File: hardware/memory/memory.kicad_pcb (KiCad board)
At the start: 2 copper layers, 77 x 77 mm, 76 parts, among them J1 Conn_Mem, J2 Conn_Power, J3 Conn_Mem_Ext, U1 74HC161, U10 74HC595, U11 74HC595, U12 74HC595, U13 74HC595, U14 74HC597, U15 74HC74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

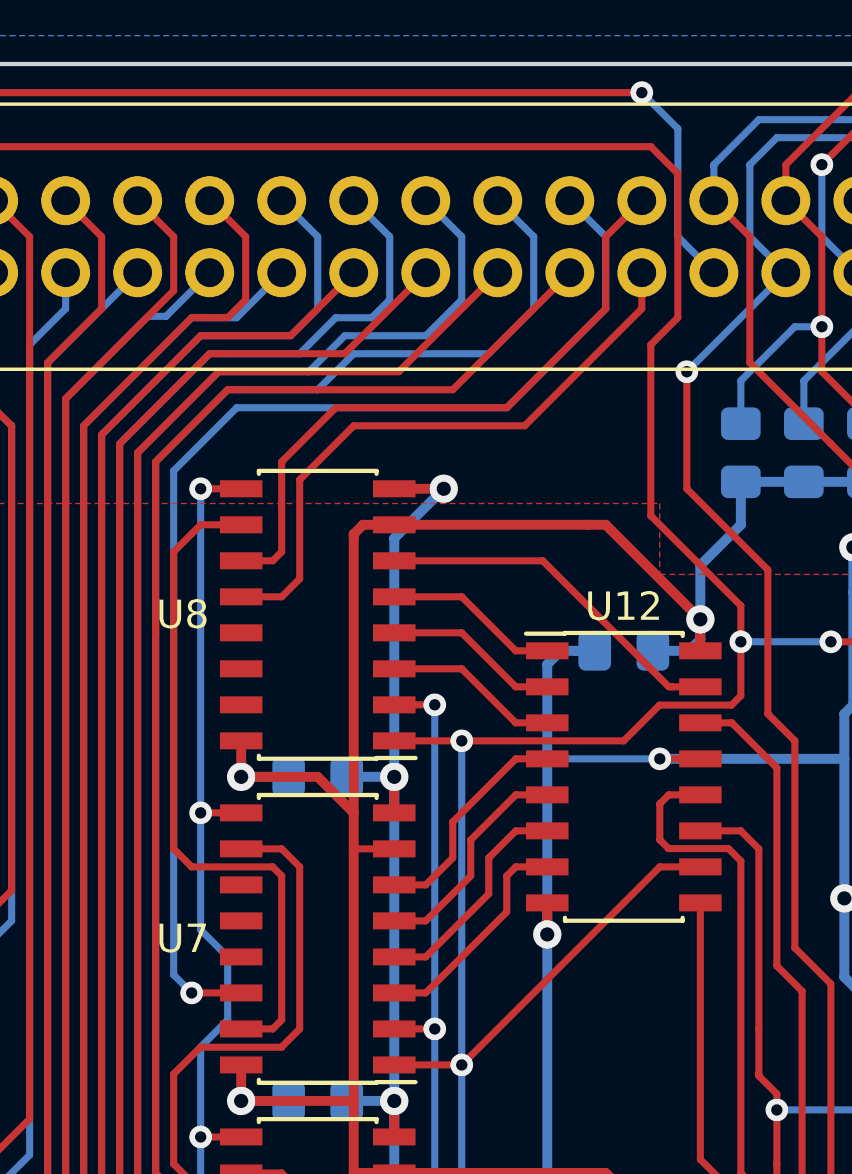
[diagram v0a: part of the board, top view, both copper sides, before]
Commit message: Added ~RESET to memory bus
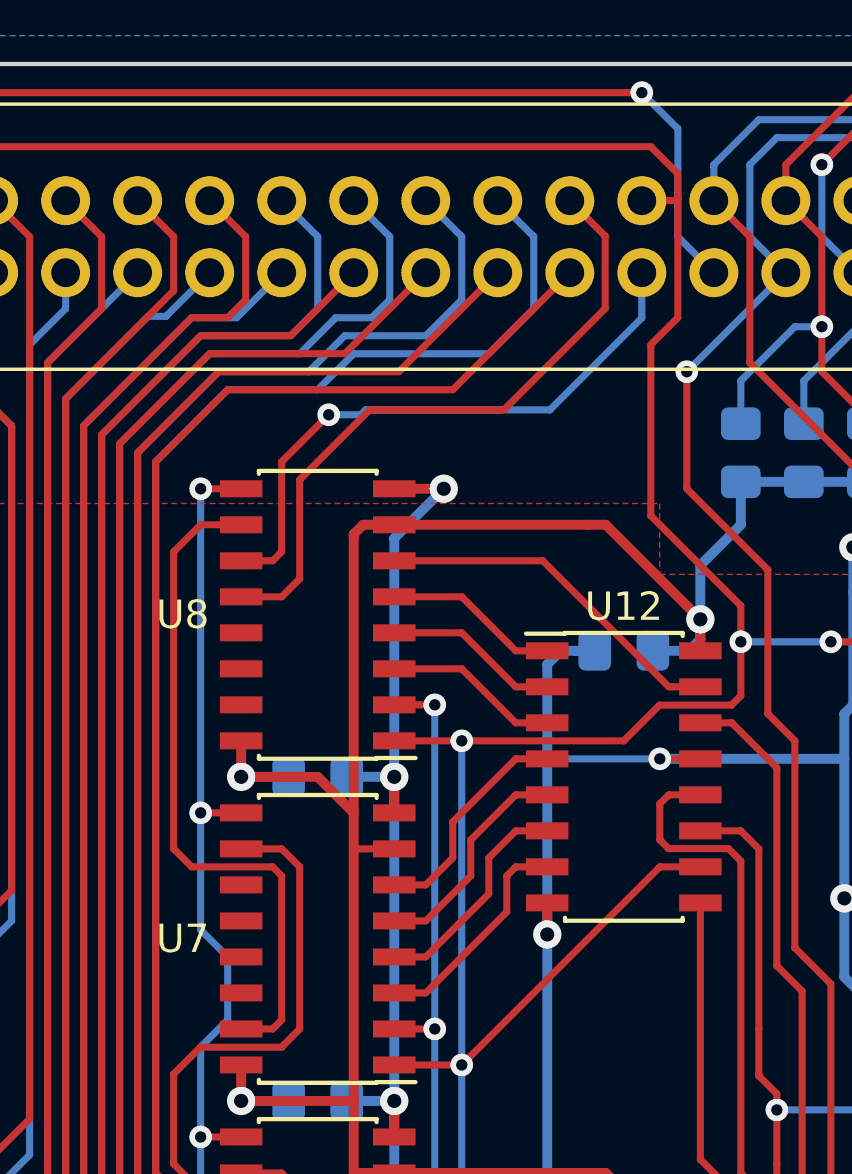
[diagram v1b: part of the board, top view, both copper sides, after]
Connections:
- J3 pad 26: /A24 -> /A30
- J3 pad 27: /A30 -> /A31
- J3 pad 28: /A31 -> /~RESET
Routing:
- net /A24: track 42.4 -> 0.00 mm, vias 1 -> 0
- net /A30: track 21.7 -> 23.4 mm
- net /A31: track 22.7 -> 21.1 mm, vias 0 -> 1
- net /~RESET: track 290.1 -> 291.4 mm
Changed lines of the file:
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@@
     (thickness 1.6)
     (drawings 17)
-    (tracks 1612)
+    (tracks 1610)
     (zones 0)
     (modules 76)
@@
       (net 102 /A23))
     (pad 26 thru_hole oval (at 2.54 30.48 90) (size 1.7272 1.7272) (drill 1.016) (layers *.Cu *.Mask)
-      (net 65 /A24))
-    (pad 27 thru_hole oval (at 0 33.02 90) (size 1.7272 1.7272) (drill 1.016) (layers *.Cu *.Mask)
       (net 57 /A30))
-    (pad 28 thru_hole oval (at 2.54 33.02 90) (size 1.7272 1.7272) (drill 1.016) (layers *.Cu *.Mask)
+    (pad 27 thru_hole oval (at 0 33.02 90) (size 1.7272 1.7272) (drill 1.016) (layers *.Cu *.Mask)
       (net 58 /A31))
+    (pad 28 thru_hole oval (at 2.54 33.02 90) (size 1.7272 1.7272) (drill 1.016) (layers *.Cu *.Mask)
+      (net 18 /~RESET))
     (pad 29 thru_hole oval (at 0 35.56 90) (size 1.7272 1.7272) (drill 1.016) (layers *.Cu *.Mask)
       (net 105 /~WAIT))
@@
   (segment (start 154.685 73.9325) (end 157.86 77.1075) (width 0.25) (layer F.Cu) (net 18))
   (segment (start 155.6375 66.9475) (end 154.685 67.9) (width 0.25) (layer F.Cu) (net 18))
-  (segment (start 155.6375 61.8675) (end 155.6375 66.9475) (width 0.25) (layer F.Cu) (net 18))
   (segment (start 154.685 67.9) (end 154.685 73.9325) (width 0.25) (layer F.Cu) (net 18))
   (segment (start 120.7125 71.075) (end 119.4425 69.805) (width 0.25) (layer F.Cu) (net 18))
@@
   (segment (start 149.3575 126.6825) (end 144.8425 126.6825) (width 0.25) (layer F.Cu) (net 18))
   (segment (start 144.2075 118.065) (end 144.2075 126.0475) (width 0.25) (layer F.Cu) (net 18))
+  (segment (start 155.6375 62.771314) (end 155.6375 62.725) (width 0.25) (layer F.Cu) (net 18))
+  (segment (start 155.588814 62.82) (end 155.6375 62.771314) (width 0.25) (layer F.Cu) (net 18))
+  (segment (start 154.3675 62.82) (end 155.588814 62.82) (width 0.25) (layer F.Cu) (net 18))
+  (segment (start 155.6375 61.8675) (end 155.6375 62.725) (width 0.25) (layer F.Cu) (net 18))
+  (segment (start 155.6375 62.725) (end 155.6375 66.9475) (width 0.25) (layer F.Cu) (net 18))
   (segment (start 156.4325 107.905) (end 159.13 107.905) (width 0.25) (layer F.Cu) (net 19))
   (segment (start 112.2975 81.235) (end 111.1875 81.235) (width 0.25) (layer F.Cu) (net 19))
@@
   (segment (start 118.49 90.76) (end 123.0925 90.76) (width 0.25) (layer F.Cu) (net 53))
   (segment (start 114.045 86.315) (end 118.49 90.76) (width 0.25) (layer F.Cu) (net 53))
-  (segment (start 141.6675 76.79) (end 140.2375 76.79) (width 0.25) (layer F.Cu) (net 57))
-  (segment (start 154.3675 65.36) (end 154.3675 66.63) (width 0.25) (layer F.Cu) (net 57))
-  (segment (start 142.3025 76.155) (end 141.6675 76.79) (width 0.25) (layer F.Cu) (net 57))
-  (segment (start 154.3675 66.63) (end 150.24 70.7575) (width 0.25) (layer F.Cu) (net 57))
-  (segment (start 150.24 70.7575) (end 144.2075 70.7575) (width 0.25) (layer F.Cu) (net 57))
-  (segment (start 144.2075 70.7575) (end 142.3025 72.6625) (width 0.25) (layer F.Cu) (net 57))
-  (segment (start 142.3025 72.6625) (end 142.3025 76.155) (width 0.25) (layer F.Cu) (net 57))
+  (segment (start 153.075 64.0675) (end 151.8275 62.82) (width 0.25) (layer F.Cu) (net 57))
+  (segment (start 153.075 66.625) (end 153.075 64.0675) (width 0.25) (layer F.Cu) (net 57))
+  (segment (start 141.6675 76.79) (end 142.3025 76.155) (width 0.25) (layer F.Cu) (net 57))
+  (segment (start 140.2375 76.79) (end 141.6675 76.79) (width 0.25) (layer F.Cu) (net 57))
+  (segment (start 142.3025 76.155) (end 142.3025 72.6625) (width 0.25) (layer F.Cu) (net 57))
+  (segment (start 144.765 70.2) (end 149.5 70.2) (width 0.25) (layer F.Cu) (net 57))
+  (segment (start 142.3025 72.6625) (end 144.765 70.2) (width 0.25) (layer F.Cu) (net 57))
+  (segment (start 149.5 70.2) (end 153.075 66.625) (width 0.25) (layer F.Cu) (net 57))
   (segment (start 141.35 75.52) (end 140.2375 75.52) (width 0.25) (layer F.Cu) (net 58))
   (segment (start 141.6675 75.2025) (end 141.35 75.52) (width 0.25) (layer F.Cu) (net 58))
-  (segment (start 154.3675 62.82) (end 153.0975 64.09) (width 0.25) (layer F.Cu) (net 58))
-  (segment (start 149.605 70.1225) (end 143.5725 70.1225) (width 0.25) (layer F.Cu) (net 58))
-  (segment (start 153.0975 66.63) (end 149.605 70.1225) (width 0.25) (layer F.Cu) (net 58))
-  (segment (start 153.0975 64.09) (end 153.0975 66.63) (width 0.25) (layer F.Cu) (net 58))
-  (segment (start 143.5725 70.1225) (end 141.6675 72.0275) (width 0.25) (layer F.Cu) (net 58))
   (segment (start 141.6675 72.0275) (end 141.6675 75.2025) (width 0.25) (layer F.Cu) (net 58))
+  (via (at 143.325 70.37) (size 0.8) (drill 0.4) (layers F.Cu B.Cu) (net 58))
+  (segment (start 143.325 70.37) (end 141.6675 72.0275) (width 0.25) (layer F.Cu) (net 58))
+  (segment (start 143.325 70.37) (end 144.455 70.37) (width 0.25) (layer B.Cu) (net 58))
+  (segment (start 144.455 70.37) (end 144.625 70.2) (width 0.25) (layer B.Cu) (net 58))
+  (segment (start 144.625 70.2) (end 151.125 70.2) (width 0.25) (layer B.Cu) (net 58))
+  (segment (start 154.3675 66.9575) (end 154.3675 65.36) (width 0.25) (layer B.Cu) (net 58))
+  (segment (start 151.125 70.2) (end 154.3675 66.9575) (width 0.25) (layer B.Cu) (net 58))
   (segment (start 138.81 74.25) (end 140.2375 74.25) (width 0.25) (layer F.Cu) (net 59))
   (segment (start 137.8575 75.2025) (end 138.81 74.25) (width 0.25) (layer F.Cu) (net 59))
@@
   (segment (start 140.2375 85.68) (end 141.6675 85.68) (width 0.25) (layer F.Cu) (net 61))
   (segment (start 142.3025 92.03) (end 142.3025 86.315) (width 0.25) (layer F.Cu) (net 61))
-  (segment (start 153.0975 64.09) (end 153.0975 66.63) (width 0.25) (layer B.Cu) (net 65))
-  (segment (start 140.08 70.1225) (end 137.8575 72.345) (width 0.25) (layer B.Cu) (net 65))
-  (segment (start 153.0975 66.63) (end 149.605 70.1225) (width 0.25) (layer B.Cu) (net 65))
-  (segment (start 151.8275 62.82) (end 153.0975 64.09) (width 0.25) (layer B.Cu) (net 65))
-  (segment (start 149.605 70.1225) (end 140.08 70.1225) (width 0.25) (layer B.Cu) (net 65))
-  (segment (start 137.8575 72.345) (end 137.8575 90.125) (width 0.25) (layer B.Cu) (net 65))
-  (segment (start 137.8575 90.125) (end 138.4925 90.76) (width 0.25) (layer B.Cu) (net 65))
-  (via (at 138.4925 90.76) (size 0.8) (drill 0.4) (layers F.Cu B.Cu) (net 65))
-  (segment (start 140.2375 90.76) (end 138.4925 90.76) (width 0.25) (layer F.Cu) (net 65))
   (segment (start 141.35 114.89) (end 140.2375 114.89) (width 0.25) (layer F.Cu) (net 66))
   (segment (start 142.3025 108.54141) (end 142.3025 113.9375) (width 0.25) (layer F.Cu) (net 66))

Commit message: Unified footprints
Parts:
- U19, U21: footprint Package_TO_SOT_SMD:SOT-23-5 -> Package_TO_SOT_SMD:SOT-23-5_HandSoldering
- moved C21 0.45 mm to (176.9, 72.8)
- moved C19 0.22 mm to (172.4, 121.4)
- moved C22 0.19 mm to (165.0, 121.4)
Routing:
- net /~MEM_WE: track 114.3 -> 116.4 mm
- net /~MEM_OE: track 132.7 -> 134.8 mm
- net VCC: track 493.6 -> 491.8 mm, vias 22 -> 20
- net GND: track 536.8 -> 535.7 mm
- net /LED_LATCH: track 20.0 -> 19.2 mm
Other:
- board text added: "2020-06-11"
- board text removed: "2020-05-29"

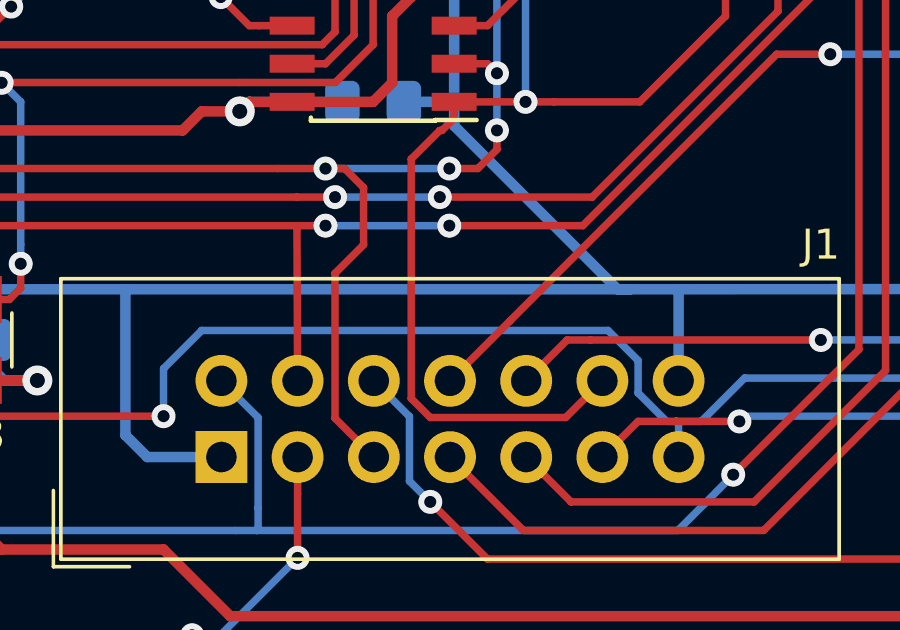
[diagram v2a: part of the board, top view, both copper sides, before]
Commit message: Added placeholders for JLCPCB serial numbers
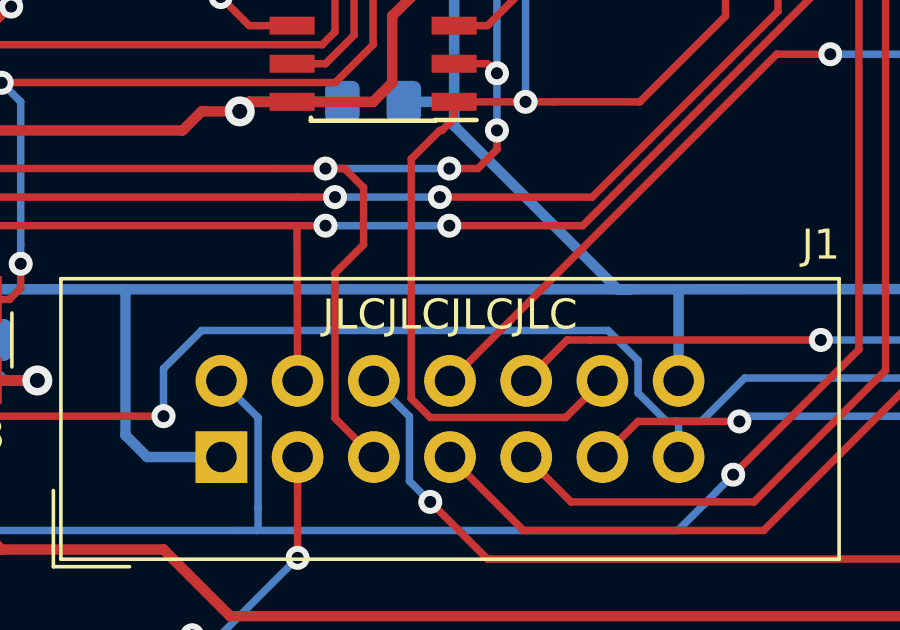
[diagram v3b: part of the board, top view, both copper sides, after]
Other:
- board text added: "JLCJLCJLCJLC"
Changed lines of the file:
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@@
   (general
     (thickness 1.6)
-    (drawings 17)
+    (drawings 18)
     (tracks 1611)
     (zones 0)
@@
       (xy 0.1016 -0.166391)) (layer B.SilkS) (width 0.01))
   )
+  (gr_text JLCJLCJLCJLC (at 145.5 123.25) (layer F.SilkS)
+    (effects (font (size 1 1) (thickness 0.15)))
+  )
   (gr_text GND (at 181.75 127) (layer B.SilkS)
